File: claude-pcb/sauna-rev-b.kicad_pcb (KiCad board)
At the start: 2 copper layers, 130 x 85 mm, 96 parts, among them Q1 AOD4184A, Q2 AOD4184A, Q3 AOD4184A, Q4 AOD4184A, Q5 AOD4184A, U1 OKI-78SR-5/1.5-W36-C, U2 USBLC6-2SC6

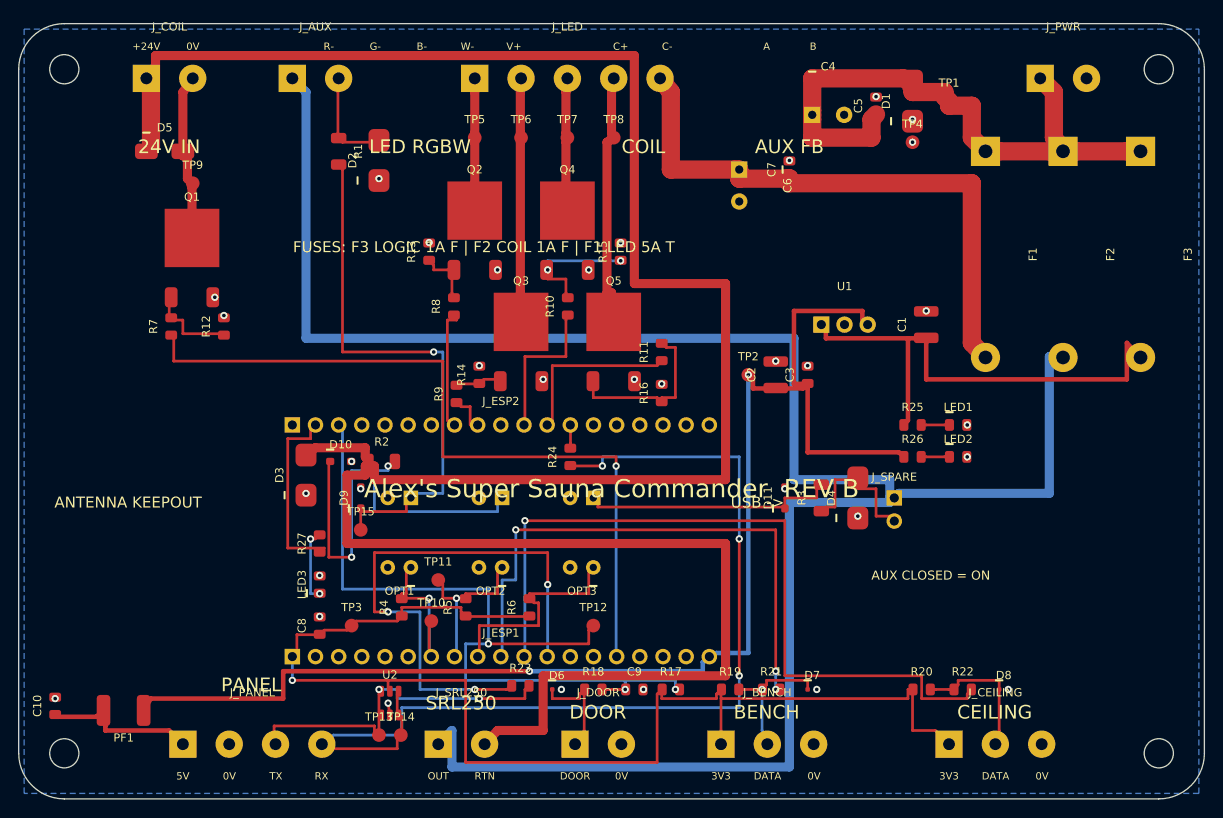
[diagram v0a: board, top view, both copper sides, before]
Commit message: Rearrange Rev B board: coil/aux on right edge, SRL bottom-right
Re-floorplan so connectors follow the physical harness, with the
contactor located to the right of the board:
- J_COIL, J_AUX moved to the right edge (next to the contactor)
- J_SRL250 to the right side of the bottom edge (sauna-room harness)
- J_PWR stays on the top edge; fuse bank below it
- J_LED to the left edge (upper-left, above the antenna keepout)
- coil MOSFET + optos cluster on the right by their connectors;
  LED MOSFETs sit by J_LED on the left

Re-placed all associated sub-circuits, re-ran the autorouter (158
routes, 68 vias, 0 failures) and the checker (clearances, courtyards,
keepout, full net connectivity all pass). Regenerated schematic and
board, refreshed silkscreen labels and the connector-plan docs.

https://claude.ai/code/session_015SfBebRXzY4tA1yHmXqVHv
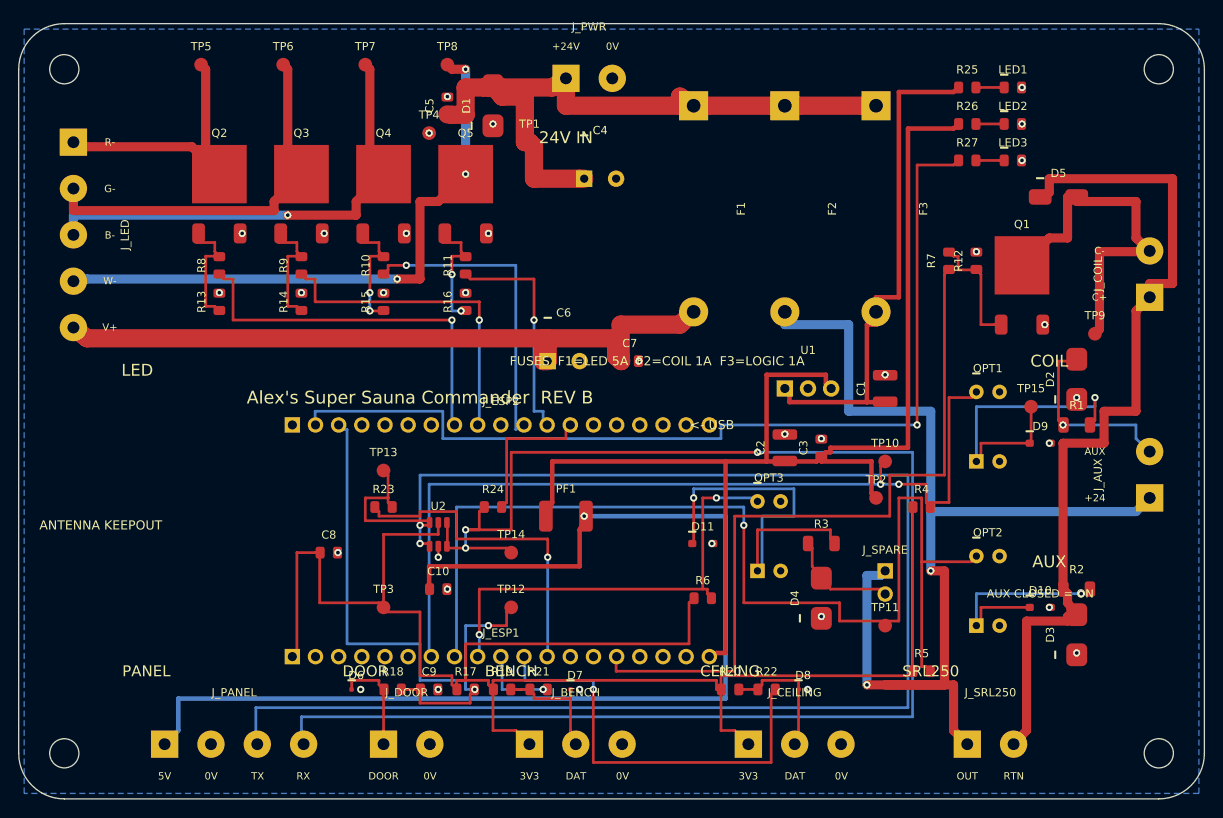
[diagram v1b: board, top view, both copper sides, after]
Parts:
- moved J_COIL 112.6 mm to (124.0, 30.0), turned to 90 degrees
- moved J_AUX 104.7 mm to (124.0, 52.0), turned to 90 degrees
- moved TP9 100.3 mm to (118.0, 34.0)
- moved D5 98.1 mm to (114.0, 19.0)
- moved Q1 91.0 mm to (110.0, 28.0)
- moved LED3 89.1 mm to (109.0, 15.0), turned to 0 degrees
- moved R1 86.3 mm to (116.0, 44.0), turned to 0 degrees
- moved D3 86.3 mm to (116.0, 67.0)
- moved R7 85.6 mm to (102.0, 26.0)
- moved R12 82.8 mm to (105.0, 26.0)
- moved R27 82.5 mm to (104.0, 15.0), turned to 0 degrees
- moved D2 80.2 mm to (116.0, 39.0)
- moved D10 78.4 mm to (112.0, 64.0)
- moved R2 77.5 mm to (116.0, 62.0)
- moved D9 74.7 mm to (112.0, 46.0), turned to 0 degrees
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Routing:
- net SRL250_RTN: track 277.7 -> 95.6 mm
- net PANEL_TX: track 38.5 -> 181.2 mm
- net +5V_PANEL: track 17.0 -> 126.0 mm, vias 0 -> 1
- net +24V_SAFE: track 229.0 -> 120.3 mm, vias 0 -> 2
- net GPIO33: track 18.3 -> 120.1 mm
- net GPIO23: track 21.2 -> 105.2 mm, vias 0 -> 1
- net GPIO32: track 17.7 -> 96.1 mm, vias 1 -> 2
- net PANEL_RX: track 111.2 -> 172.8 mm
- net GPIO26: track 61.9 -> 8.57 mm, vias 3 -> 1
- net +3V3: track 137.1 -> 184.5 mm, vias 1 -> 0
- net LED_W-: track 27.7 -> 66.5 mm, vias 0 -> 3
- net GPIO27: track 84.1 -> 46.8 mm
- net LED_B-: track 14.6 -> 51.5 mm, vias 0 -> 1
- net GPIO18: track 4.49 -> 35.8 mm, vias 0 -> 1
- net GPIO19: track 13.5 -> 41.8 mm, vias 0 -> 1
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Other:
- board text added: "+24"
- board text added: "<- USB"
- board text added: "AUX"
- board text added: "DAT"
- board text added: "FUSES F1=LED 5A F2=COIL 1A F3=LOGIC 1A"
- board text added: "LED"
- board text removed: "A"
- board text removed: "AUX FB"
- board text removed: "B"
- board text removed: "DATA"
- board text removed: "FUSES: F3 LOGIC 1A F | F2 COIL 1A F | F1 LED 5A T"
- board text removed: "LED RGBW"
- board text removed: "USB ->"
